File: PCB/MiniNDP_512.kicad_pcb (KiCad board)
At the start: 2 copper layers, 60 x 34 mm, 26 parts, among them J1 Conn_02x20_Odd_Even, M1 MountHole_M2.5, M2 MountHole_M2.5, M3 MountHole_M2.5, M4 MountHole_M2.5, U1 74161, U2 74161, U3 74161, U4 74138, U5 74374, U6 AS6C4008_TSOP, U7 1G32, U8 1G08

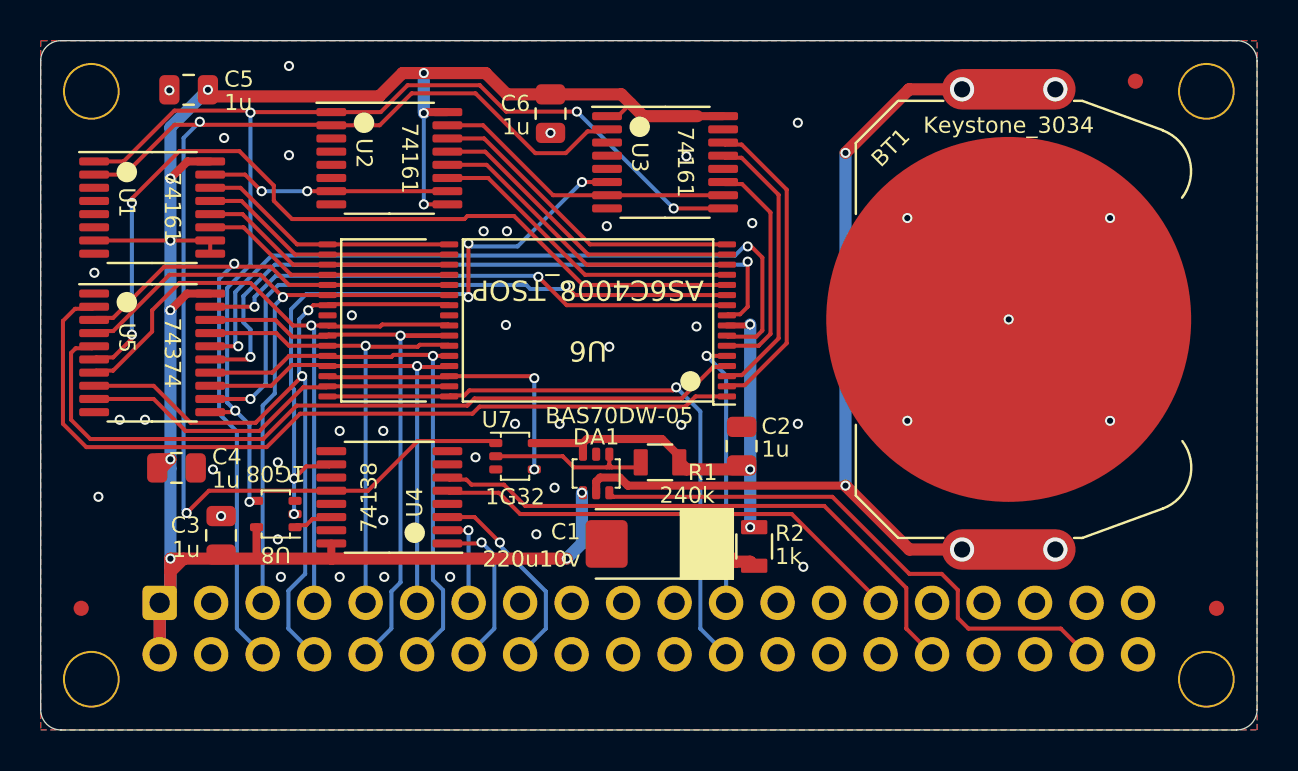
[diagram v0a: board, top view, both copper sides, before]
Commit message: 512k support
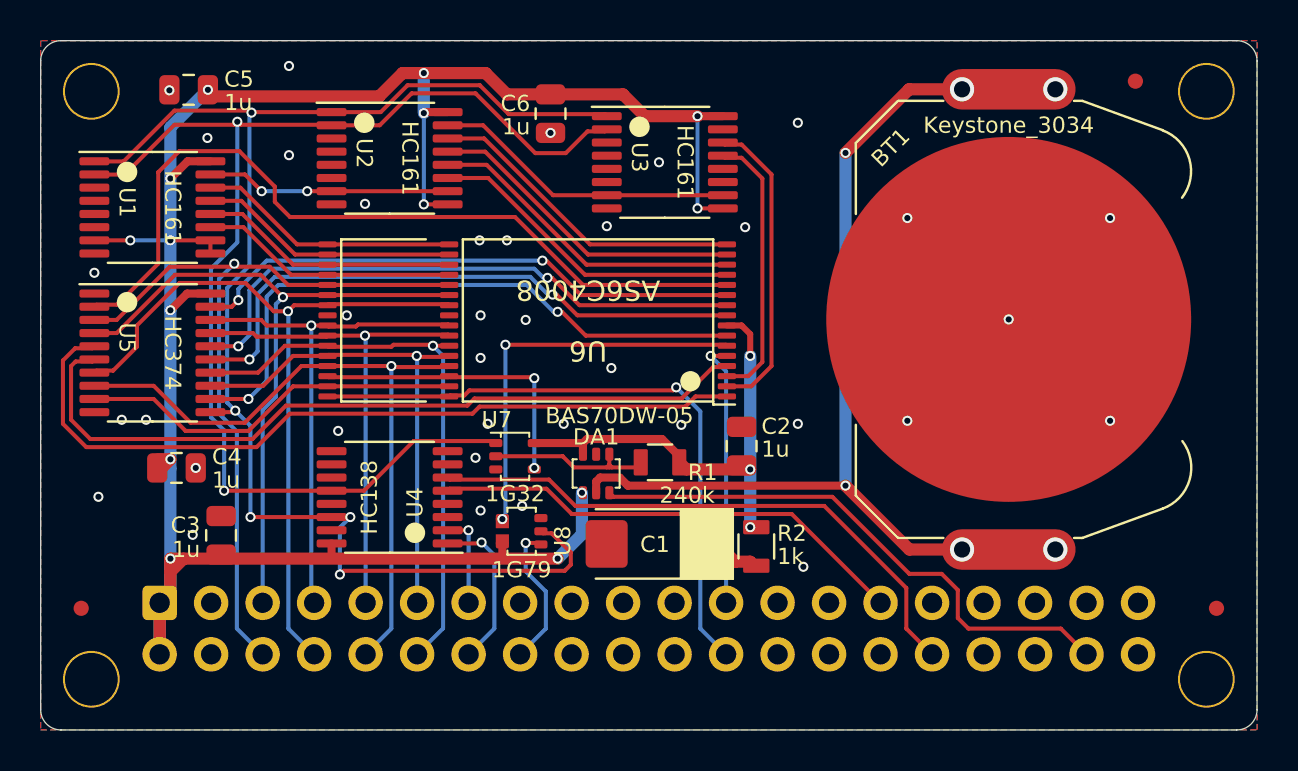
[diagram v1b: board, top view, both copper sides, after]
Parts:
- added JP1: 256k, 000_LOCAL:SolderJumper-2_Open 0.65mm, F.Cu at (144.7, 110.2)
- U1, U2, U3: value 74161 -> HC161
- U4: value 74138 -> HC138
- U5: value 74374 -> HC374
- U6: value AS6C4008_TSOP -> AS6C4008
- U8: value 1G08 -> 1G79
- moved U8 12.2 mm to (145.7, 110.2)
- moved R2 0.10 mm to (157.2, 111.0)
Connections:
- net /CARRY0 renamed /TC0
- net /CARRY1 renamed /TC1
- U1 pad 11: /A0 -> /A3
- U1 pad 12: /A1 -> /A2
- U1 pad 13: /A2 -> /A1
- U1 pad 14: /A3 -> /A0
- U3 pad 1: VBUS -> /~{BLOCK}
- U3 pad 11: /A18 -> unconnected-(U3-Q3-Pad11)
- U3 pad 6: /~{BANK} -> GND
- U3 pad 9: /~{BLOCK} -> VBUS
- U4 pad 10: /~{BANK} -> unconnected-(U4-O5-Pad10)
- U4 pad 14: Net-(U4-O1) -> /~{BLOCK}
- U4 pad 3: /BUS_A10 -> GND
- U5 pad 15: /A17 -> /A15
- U5 pad 16: /A15 -> /A16
- U5 pad 18: /AD4 -> /AD3
- U5 pad 19: /A16 -> /A17
- U5 pad 2: /A11 -> /A10
- U5 pad 5: /A13 -> /A11
- U5 pad 7: /AD3 -> /AD2
- U5 pad 8: /AD2 -> /AD4
- U5 pad 9: /A10 -> /A13
- U6 pad 11: /A14 -> /A17
- U6 pad 12: /A12 -> /A10
- U6 pad 17: /A3 -> /A0
- U6 pad 18: /A2 -> /A1
- U6 pad 19: /A1 -> /A2
- U6 pad 20: /A0 -> /A3
- U6 pad 26: /AD4 -> /AD5
- U6 pad 27: /AD5 -> /AD6
- U6 pad 28: /AD6 -> /AD7
- U6 pad 29: /AD7 -> /AD4
- U6 pad 31: /A10 -> /A13
- U6 pad 4: /A13 -> /A12
- U6 pad 7: /A15 -> /A14
- U6 pad 9: /A17 -> /A15
- U8 pad 1: Net-(U4-O1) -> /BUS_A10
- U8 pad 2: /~{BANK} -> /~{BLOCK}
- U8 pad 4: /~{BLOCK} -> /A18
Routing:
- net /~{BANK}: track 32.3 -> 0.00 mm, vias 5 -> 0
- net /A10: track 19.1 -> 40.2 mm
- net /A13: track 38.8 -> 19.1 mm
- net /~{BLOCK}: track 57.0 -> 71.8 mm
- net /AD3: track 34.7 -> 25.7 mm
- net /A18: track 11.3 -> 19.9 mm, vias 0 -> 2
- net /A15: track 36.8 -> 29.6 mm
- net /A17: track 34.2 -> 27.4 mm
- net /A12: track 42.8 -> 38.2 mm, vias 2 -> 0
- net VBUS: track 109.8 -> 113.0 mm, vias 11 -> 14
- net /AD4: track 31.0 -> 34.2 mm
- net /~{BYTE}: track 65.3 -> 62.3 mm
- net /BUS_A10: track 10.1 -> 7.21 mm
- net /A16: track 27.0 -> 29.1 mm
- net Net-(U4-O1): track 1.99 -> 0.00 mm
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
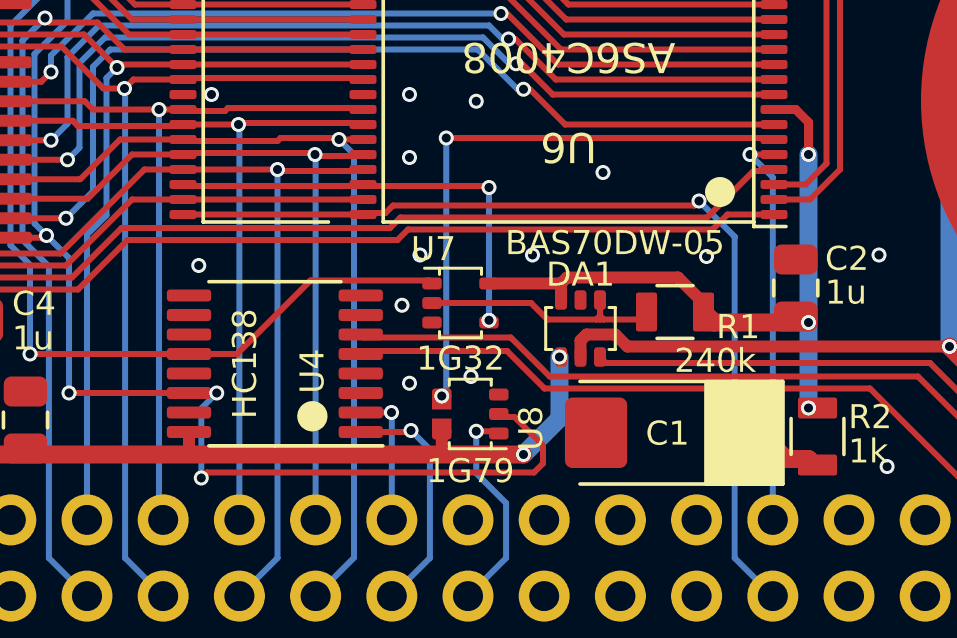
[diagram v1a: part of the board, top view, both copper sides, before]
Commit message: minindp small cosmetic adjustments
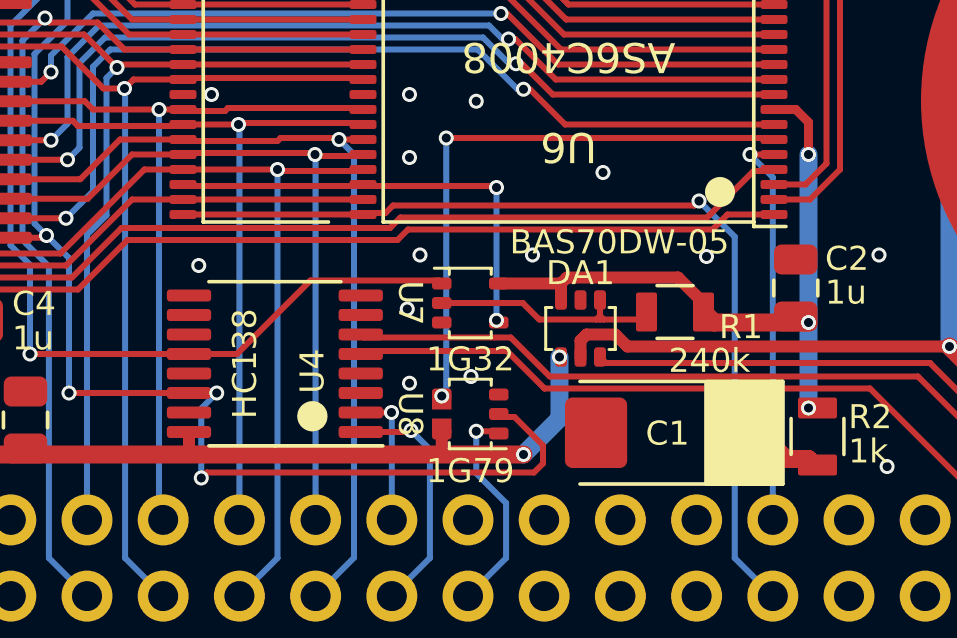
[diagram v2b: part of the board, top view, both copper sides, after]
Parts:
- moved U7 0.33 mm to (145.7, 106.5)

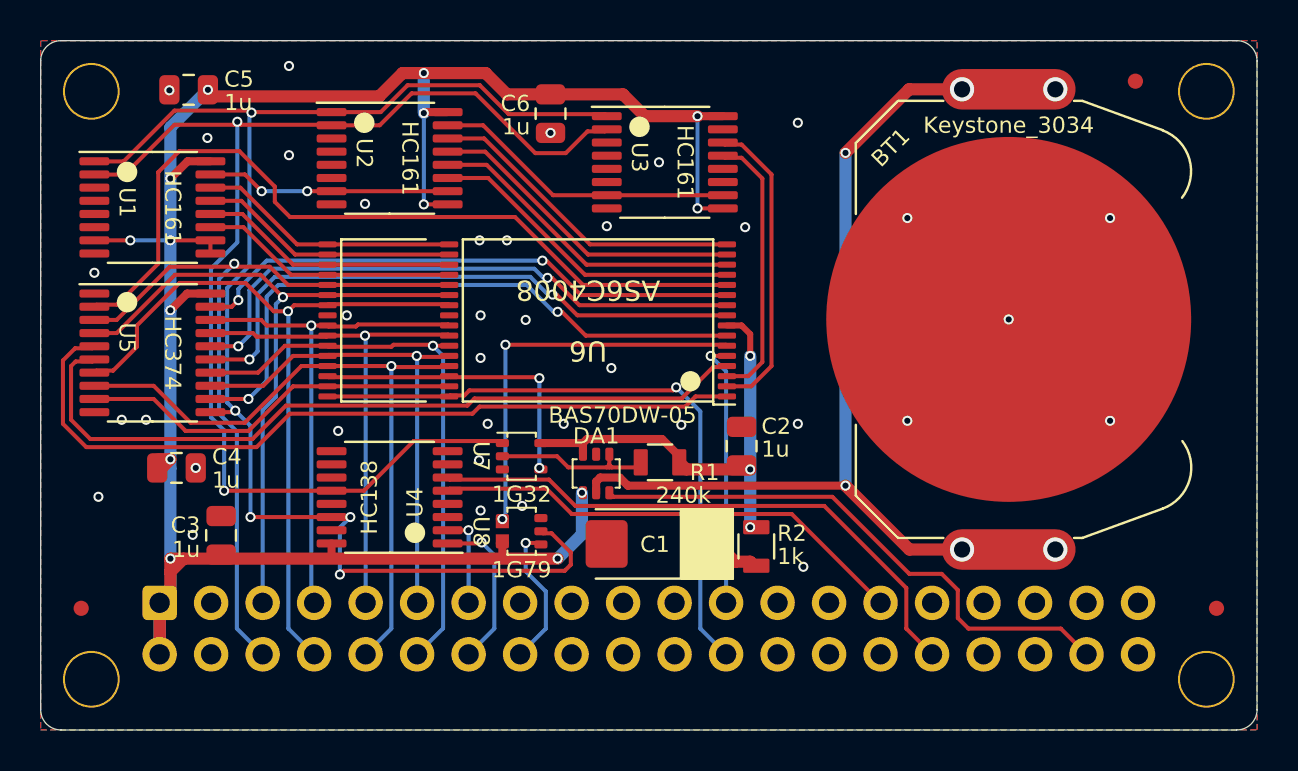
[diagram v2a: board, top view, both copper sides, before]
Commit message: add experimental 1 megabyte MiniNDP 1M
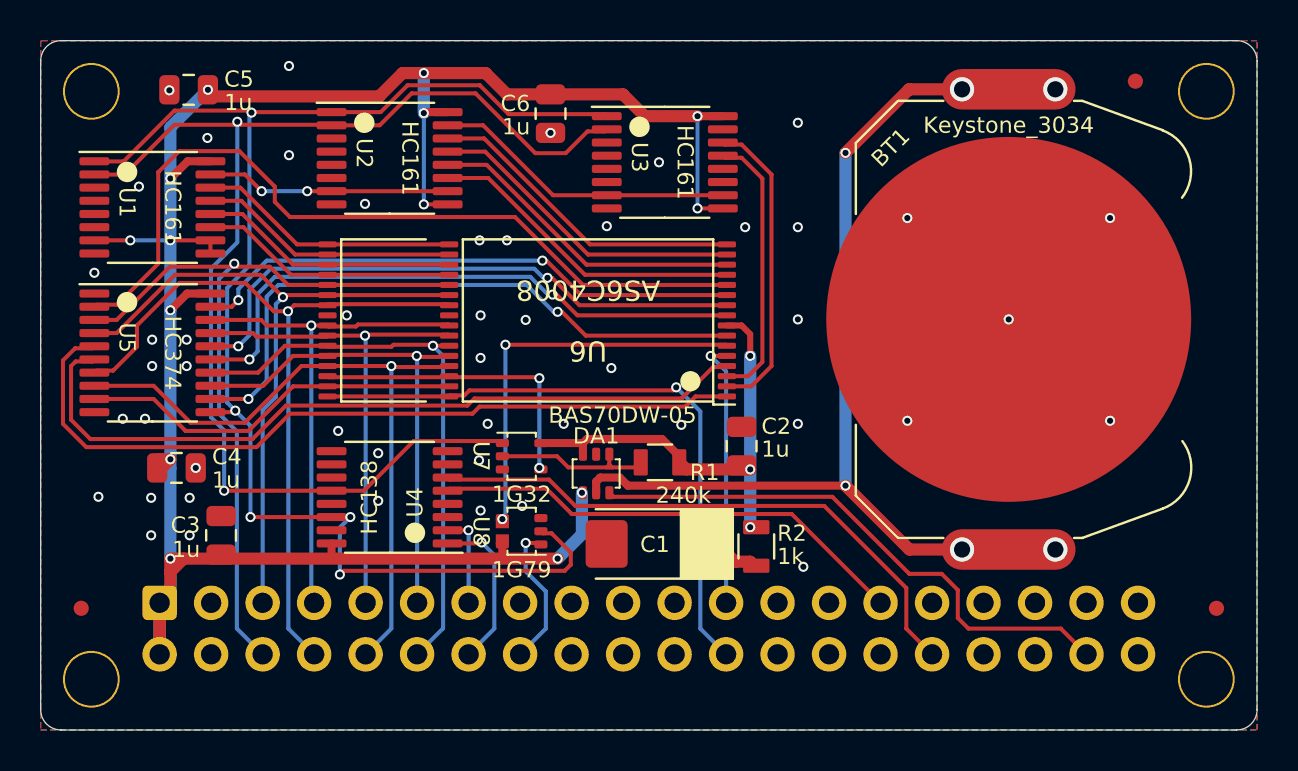
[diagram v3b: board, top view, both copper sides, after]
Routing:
- net GND: vias 37 -> 49

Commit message: Redraw 1M for SOIC-24 FCT821, 2mm corners, remove corner holes, update cover
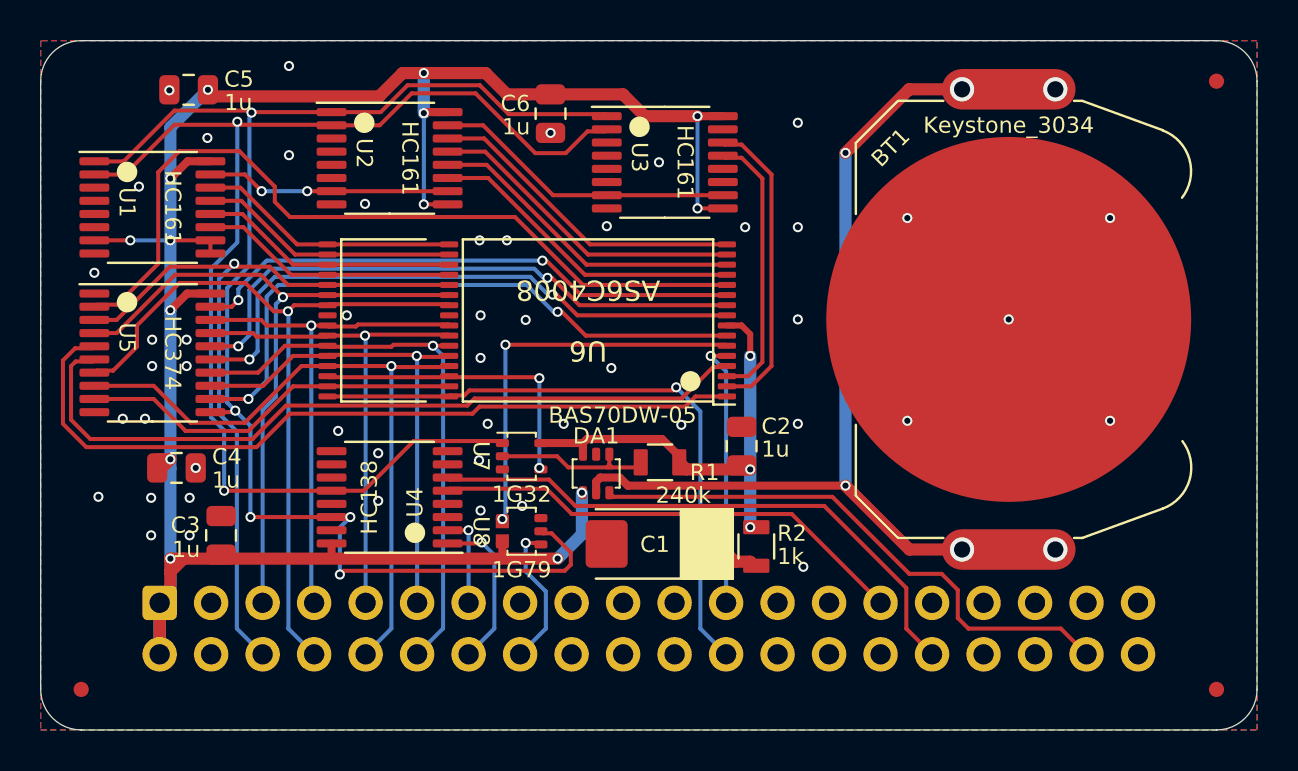
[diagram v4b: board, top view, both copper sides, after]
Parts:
- removed F1, F2: Fiducial_0.75_1.5, 000_LOCAL:Fiducial_0.75_1.5
- removed M1, M2, M3, M4: MountHole_M2.5, 000_LOCAL:MountHole_M2.5
- added F3: Fiducial_0.75_1.5, 000_LOCAL:Fiducial_0.75_1.5, F.Cu at (179.9, 88.0)
- added F3: Fiducial_0.75_1.5, 000_LOCAL:Fiducial_0.75_1.5, F.Cu at (179.9, 118.0)
- moved F3 4.00 mm to (124.0, 118.0)
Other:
- outline, holes or cut-outs redrawn

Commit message: routing and enclosure tweaks
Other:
- board text added: "cover"
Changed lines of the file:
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@@
 	)
 	(gr_line
+		(start 154.45 118.35)
+		(end 154.45 119.1)
+		(stroke
+			(width 0.05)
+			(type default)
+		)
+		(layer "Dwgs.User")
+	)
+	(gr_line
+		(start 123.95 119.225)
+		(end 179.95 119.225)
+		(stroke
+			(width 0.02)
+			(type default)
+		)
+		(layer "Dwgs.User")
+	)
+	(gr_arc
+		(start 122.75 88.025)
+		(mid 123.101472 87.176472)
+		(end 123.95 86.825)
+		(stroke
+			(width 0.02)
+			(type default)
+		)
+		(layer "Dwgs.User")
+	)
+	(gr_line
+		(start 154.45 119.1)
+		(end 154.25 118.9)
+		(stroke
+			(width 0.05)
+			(type default)
+		)
+		(layer "Dwgs.User")
+	)
+	(gr_line
+		(start 122.75 88.025)
+		(end 122.75 118.025)
+		(stroke
+			(width 0.02)
+			(type default)
+		)
+		(layer "Dwgs.User")
+	)
+	(gr_arc
+		(start 123.95 119.225)
+		(mid 123.101472 118.873528)
+		(end 122.75 118.025)
+		(stroke
+			(width 0.02)
+			(type default)
+		)
+		(layer "Dwgs.User")
+	)
+	(gr_arc
+		(start 179.95 86.825)
+		(mid 180.798528 87.176472)
+		(end 181.15 88.025)
+		(stroke
+			(width 0.02)
+			(type default)
+		)
+		(layer "Dwgs.User")
+	)
+	(gr_line
+		(start 123.95 86.825)
+		(end 179.95 86.825)
+		(stroke
+			(width 0.02)
+			(type default)
+		)
+		(layer "Dwgs.User")
+	)
+	(gr_line
+		(start 181.15 88.025)
+		(end 181.15 118.025)
+		(stroke
+			(width 0.02)
+			(type default)
+		)
+		(layer "Dwgs.User")
+	)
+	(gr_arc
+		(start 181.15 118.025)
+		(mid 180.798528 118.873528)
+		(end 179.95 119.225)
+		(stroke
+			(width 0.02)
+			(type default)
+		)
+		(layer "Dwgs.User")
+	)
+	(gr_line
+		(start 154.45 119.1)
+		(end 154.65 118.9)
+		(stroke
+			(width 0.05)
+			(type default)
+		)
+		(layer "Dwgs.User")
+	)
+	(gr_line
 		(start 123.95 86.025)
 		(end 179.95 86.025)
@@
 		)
 	)
+	(gr_text "cover"
+		(at 151.95 118.625 0)
+		(layer "Dwgs.User")
+		(effects
+			(font
+				(size 1 1)
+				(thickness 0.05)
+			)
+		)
+	)
 	(via
 		(at 136.625 105.275)
@@
 		)
 	)
+	(group ""
+		(members "2377220b-e04d-4b81-ac5a-a1b9f679845b" "293695ee-931b-4bc5-802d-b60be26dd645"
+			"3cec5b49-d6fa-4a27-8fc8-465a14676a6e" "3e78ce8d-5c23-4b43-bf3c-0a43a453ad55"
+			"444327b1-bdaa-4f00-8a88-f7abaaed7b07" "4880f06d-8220-493e-81e7-b1eaa7b5cd00"
+			"654ecf28-9388-4528-9a5e-542e15eab4d2" "c91c7ba7-5c10-43f0-8d03-23363b4ac31e"
+		)
+	)
+	(group ""
+		(members "110f3e97-3c1a-4353-8aa6-3fb432e7f7e0" "3a0487a2-6598-46ce-a8ad-5697dcb2f4ef"
+			"dbcedae4-68f0-4303-a590-17a9a76ad364"
+		)
+	)

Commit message: 1M_B & 512_B
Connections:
- net /BATT+ renamed +BATT

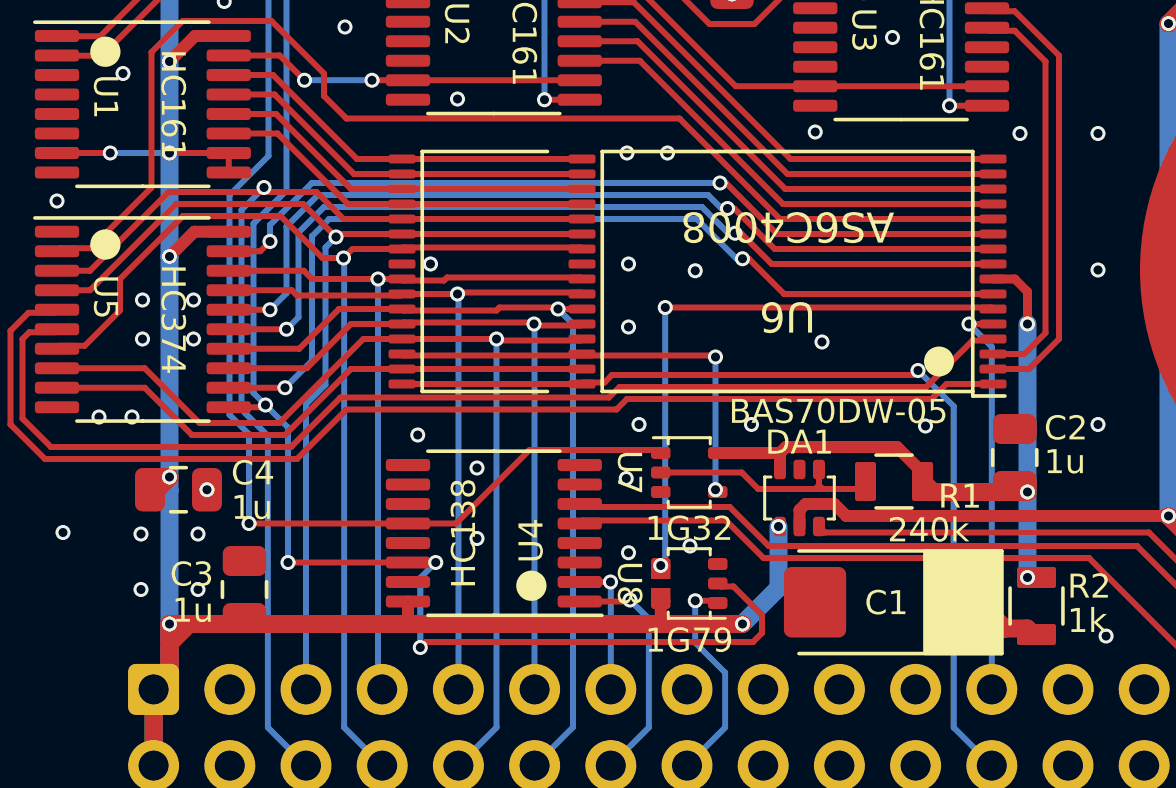
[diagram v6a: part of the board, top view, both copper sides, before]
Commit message: fix 128k compatibility, AD7->A17->pin9
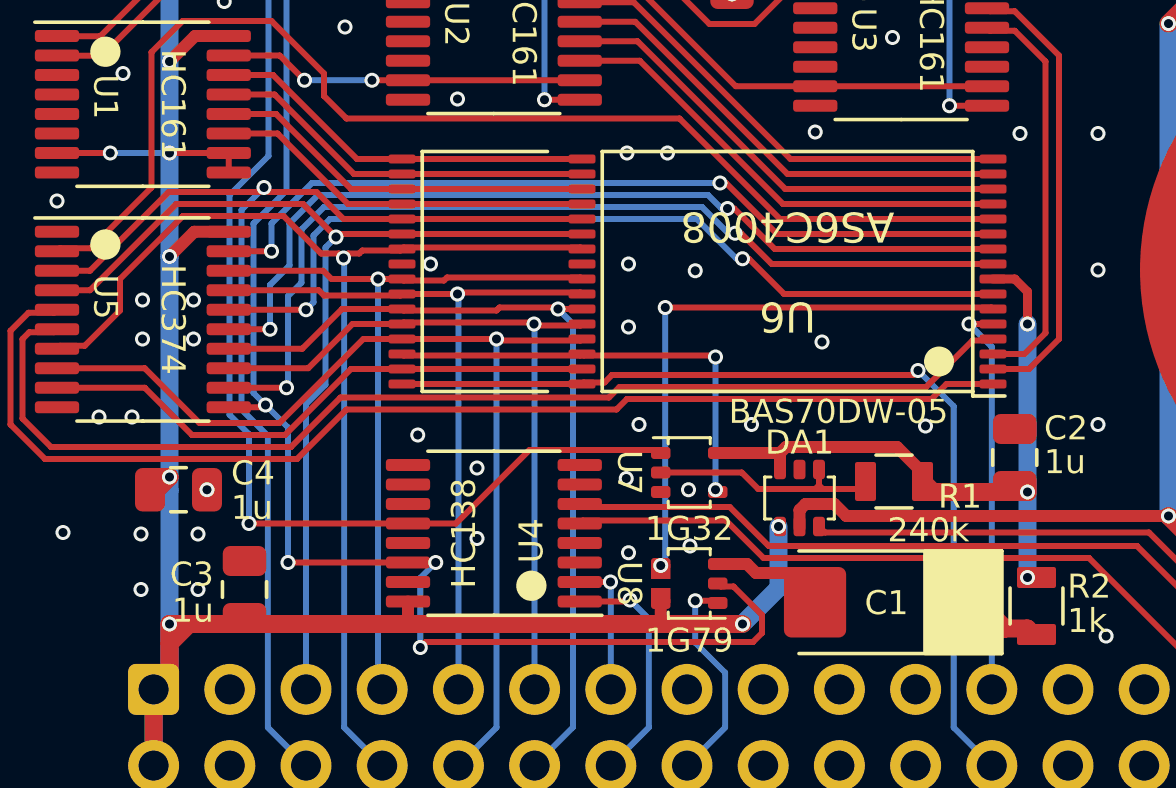
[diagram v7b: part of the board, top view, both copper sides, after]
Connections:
- U5 pad 12: /A14 -> /A17
- U5 pad 15: /A15 -> /A16
- U5 pad 16: /A16 -> /A15
- U5 pad 19: /A17 -> /A13
- U5 pad 9: /A13 -> /A14
- U6 pad 11: /A17 -> /A13
- U6 pad 31: /A13 -> /A14
- U6 pad 7: /A14 -> /A15
- U6 pad 9: /A15 -> /A17
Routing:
- net /A14: track 31.3 -> 19.1 mm, vias 2 -> 0
- net /A13: track 19.1 -> 27.7 mm, vias 0 -> 2
- net GND: track 0.00 -> 4.34 mm, vias 49 -> 50
- net /A17: track 27.4 -> 31.6 mm
- net /A16: track 29.1 -> 29.8 mm
- net /A15: track 29.6 -> 29.1 mm
